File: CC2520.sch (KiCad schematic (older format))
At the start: 29 parts, among them P3 SMA_SMD, U6 CC2520, U7 CC2592, X1 32Mhz

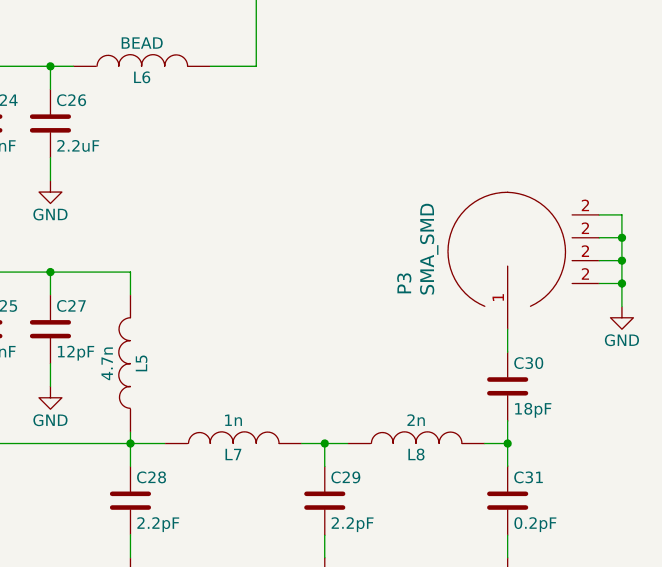
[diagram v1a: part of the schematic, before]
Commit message: tuned rf
added u.fl connectors to tune line 
moved some lines under rf components
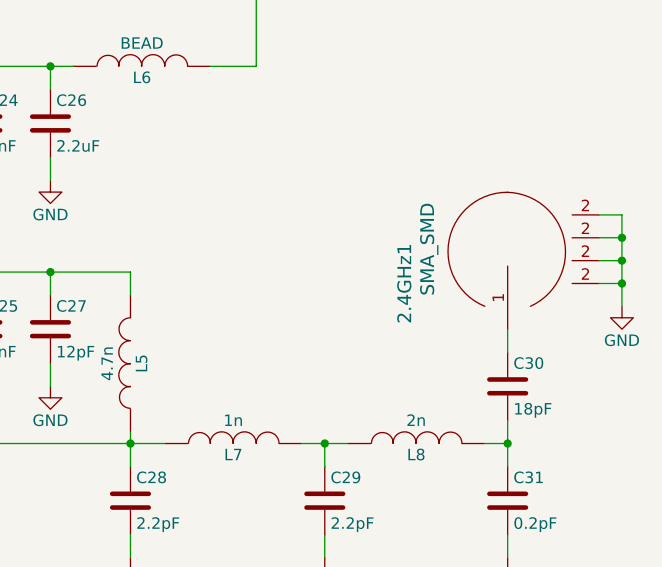
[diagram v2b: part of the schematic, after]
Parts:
- C20, C23, C26, C28, C29: footprint Capacitors_SMD:C_0402 -> Capacitor_SMD:C_0603_1608Metric
- C22, C27: footprint Capacitors_SMD:C_0402 -> Capacitor_SMD:C_1210_3225Metric
- renumbered P3 to 2.4GHz1
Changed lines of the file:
@@
 $EndComp
 $Comp
-L GND #PWR078
+L GND #PWR079
 U 1 1 5AF17357
 P 3350 1700
-F 0 "#PWR078" H 3350 1450 50  0001 C CNN
+F 0 "#PWR079" H 3350 1450 50  0001 C CNN
 F 1 "GND" H 3350 1550 50  0000 C CNN
 F 2 "" H 3350 1700 50  0001 C CNN
@@
 $EndComp
 $Comp
-L GND #PWR079
+L GND #PWR080
 U 1 1 5AF17476
 P 3700 1700
-F 0 "#PWR079" H 3700 1450 50  0001 C CNN
+F 0 "#PWR080" H 3700 1450 50  0001 C CNN
 F 1 "GND" H 3700 1550 50  0000 C CNN
 F 2 "" H 3700 1700 50  0001 C CNN
@@
 $EndComp
 $Comp
-L GND #PWR080
+L GND #PWR081
 U 1 1 5AF174E2
 P 4050 1700
-F 0 "#PWR080" H 4050 1450 50  0001 C CNN
+F 0 "#PWR081" H 4050 1450 50  0001 C CNN
 F 1 "GND" H 4050 1550 50  0000 C CNN
 F 2 "" H 4050 1700 50  0001 C CNN
@@
 F 0 "C20" H 4375 1600 50  0000 L CNN
 F 1 "2.2uF" H 4375 1400 50  0000 L CNN
-F 2 "Capacitors_SMD:C_0402" H 4388 1350 50  0001 C CNN
+F 2 "Capacitor_SMD:C_0603_1608Metric" H 4388 1350 50  0001 C CNN
 F 3 "" H 4350 1500 50  0001 C CNN
 	1    4350 1500
@@
 $EndComp
 $Comp
-L GND #PWR081
+L GND #PWR082
 U 1 1 5AF17781
 P 4350 1700
-F 0 "#PWR081" H 4350 1450 50  0001 C CNN
+F 0 "#PWR082" H 4350 1450 50  0001 C CNN
 F 1 "GND" H 4350 1550 50  0000 C CNN
 F 2 "" H 4350 1700 50  0001 C CNN
@@
 $EndComp
 $Comp
-L GND #PWR082
+L GND #PWR083
 U 1 1 5AF17924
 P 3200 4700
-F 0 "#PWR082" H 3200 4450 50  0001 C CNN
+F 0 "#PWR083" H 3200 4450 50  0001 C CNN
 F 1 "GND" H 3200 4550 50  0000 C CNN
 F 2 "" H 3200 4700 50  0001 C CNN
@@
 $EndComp
 $Comp
-L GND #PWR083
+L GND #PWR084
 U 1 1 5AF17A42
 P 3600 4850
-F 0 "#PWR083" H 3600 4600 50  0001 C CNN
+F 0 "#PWR084" H 3600 4600 50  0001 C CNN
 F 1 "GND" H 3600 4700 50  0000 C CNN
 F 2 "" H 3600 4850 50  0001 C CNN
@@
 $EndComp
 $Comp
-L GND #PWR084
+L GND #PWR085
 U 1 1 5AF17F39
 P 4200 4850
-F 0 "#PWR084" H 4200 4600 50  0001 C CNN
+F 0 "#PWR085" H 4200 4600 50  0001 C CNN
 F 1 "GND" H 4200 4700 50  0000 C CNN
 F 2 "" H 4200 4850 50  0001 C CNN
@@
 $EndComp
 $Comp
-L GND #PWR085
+L GND #PWR086
 U 1 1 5AF1813C
 P 3900 4650
-F 0 "#PWR085" H 3900 4400 50  0001 C CNN
+F 0 "#PWR086" H 3900 4400 50  0001 C CNN
 F 1 "GND" H 3900 4500 50  0000 C CNN
 F 2 "" H 3900 4650 50  0001 C CNN
@@
 LNA_EN
 $Comp
-L GND #PWR086
+L GND #PWR087
 U 1 1 5AF19B73
 P 4500 4250
-F 0 "#PWR086" H 4500 4000 50  0001 C CNN
+F 0 "#PWR087" H 4500 4000 50  0001 C CNN
 F 1 "GND" H 4500 4100 50  0000 C CNN
 F 2 "" H 4500 4250 50  0001 C CNN
@@
 NoConn ~ 3100 2950
 $Comp
-L GND #PWR087
+L GND #PWR088
 U 1 1 5AF1A852
 P 1700 4300
-F 0 "#PWR087" H 1700 4050 50  0001 C CNN
+F 0 "#PWR088" H 1700 4050 50  0001 C CNN
 F 1 "GND" H 1700 4150 50  0000 C CNN
 F 2 "" H 1700 4300 50  0001 C CNN
@@
 LNA_EN
 $Comp
-L GND #PWR088
+L GND #PWR089
 U 1 1 5AF1AD36
 P 5300 4400
-F 0 "#PWR088" H 5300 4150 50  0001 C CNN
+F 0 "#PWR089" H 5300 4150 50  0001 C CNN
 F 1 "GND" H 5300 4250 50  0000 C CNN
 F 2 "" H 5300 4400 50  0001 C CNN
@@
 $EndComp
 $Comp
-L GND #PWR089
+L GND #PWR090
 U 1 1 5AF1B0D0
 P 6650 4400
-F 0 "#PWR089" H 6650 4150 50  0001 C CNN
+F 0 "#PWR090" H 6650 4150 50  0001 C CNN
 F 1 "GND" H 6650 4250 50  0000 C CNN
 F 2 "" H 6650 4400 50  0001 C CNN
@@
 $EndComp
 $Comp
-L GND #PWR090
+L GND #PWR091
 U 1 1 5AF1B236
 P 5050 4450
-F 0 "#PWR090" H 5050 4200 50  0001 C CNN
+F 0 "#PWR091" H 5050 4200 50  0001 C CNN
 F 1 "GND" H 5050 4300 50  0000 C CNN
 F 2 "" H 5050 4450 50  0001 C CNN
@@
 $EndComp
 $Comp
-L SMA_SMD P3
+L SMA_SMD 2.4GHz1
 U 1 1 5AF1C19E
 P 9600 3000
-F 0 "P3" H 9550 3450 60  0000 C CNN
+F 0 "2.4GHz1" H 9550 3450 60  0000 C CNN
 F 1 "SMA_SMD" H 9700 3350 60  0000 C CNN
 F 2 "Connectors:SMA_THT_Jack_Straight" H 9700 3550 60  0001 C CNN
@@
 F 0 "C23" H 7025 3350 50  0000 L CNN
 F 1 "2.2uF" H 7025 3150 50  0000 L CNN
-F 2 "Capacitors_SMD:C_0402" H 7038 3100 50  0001 C CNN
+F 2 "Capacitor_SMD:C_0603_1608Metric" H 7038 3100 50  0001 C CNN
 F 3 "" H 7000 3250 50  0001 C CNN
 	1    7000 3250
@@
 F 0 "C27" H 7625 3350 50  0000 L CNN
 F 1 "12pF" H 7625 3150 50  0000 L CNN
-F 2 "Capacitors_SMD:C_0402" H 7638 3100 50  0001 C CNN
+F 2 "Capacitor_SMD:C_1210_3225Metric" H 7638 3100 50  0001 C CNN
 F 3 "" H 7600 3250 50  0001 C CNN
 	1    7600 3250
@@
 F 0 "C28" H 7975 4100 50  0000 L CNN
 F 1 "2.2pF" H 7975 3900 50  0000 L CNN
-F 2 "Capacitors_SMD:C_0402" H 7988 3850 50  0001 C CNN
+F 2 "Capacitor_SMD:C_0603_1608Metric" H 7988 3850 50  0001 C CNN
 F 3 "" H 7950 4000 50  0001 C CNN
 	1    7950 4000
@@
 F 0 "C29" H 8825 4100 50  0000 L CNN
 F 1 "2.2pF" H 8825 3900 50  0000 L CNN
-F 2 "Capacitors_SMD:C_0402" H 8838 3850 50  0001 C CNN
+F 2 "Capacitor_SMD:C_0603_1608Metric" H 8838 3850 50  0001 C CNN
 F 3 "" H 8800 4000 50  0001 C CNN
 	1    8800 4000
@@
 $EndComp
 $Comp
-L GND #PWR091
+L GND #PWR092
 U 1 1 5AF1D3FB
 P 7000 3500
-F 0 "#PWR091" H 7000 3250 50  0001 C CNN
+F 0 "#PWR092" H 7000 3250 50  0001 C CNN
 F 1 "GND" H 7000 3350 50  0000 C CNN
 F 2 "" H 7000 3500 50  0001 C CNN
@@
 $EndComp
 $Comp
-L GND #PWR092
+L GND #PWR093
 U 1 1 5AF1D441
 P 7300 3500
-F 0 "#PWR092" H 7300 3250 50  0001 C CNN
+F 0 "#PWR093" H 7300 3250 50  0001 C CNN
 F 1 "GND" H 7300 3350 50  0000 C CNN
 F 2 "" H 7300 3500 50  0001 C CNN
@@
 $EndComp
 $Comp
-L GND #PWR093
+L GND #PWR094
 U 1 1 5AF1D487
 P 7600 3500
-F 0 "#PWR093" H 7600 3250 50  0001 C CNN
+F 0 "#PWR094" H 7600 3250 50  0001 C CNN
 F 1 "GND" H 7600 3350 50  0000 C CNN
 F 2 "" H 7600 3500 50  0001 C CNN
@@
 $EndComp
 $Comp
-L GND #PWR094
+L GND #PWR095
 U 1 1 5AF1DC67
 P 7950 4250
-F 0 "#PWR094" H 7950 4000 50  0001 C CNN
+F 0 "#PWR095" H 7950 4000 50  0001 C CNN
 F 1 "GND" H 7950 4100 50  0000 C CNN
 F 2 "" H 7950 4250 50  0001 C CNN
@@
 $EndComp
 $Comp
-L GND #PWR095
+L GND #PWR096
 U 1 1 5AF1DCAD
 P 8800 4250
-F 0 "#PWR095" H 8800 4000 50  0001 C CNN
+F 0 "#PWR096" H 8800 4000 50  0001 C CNN
 F 1 "GND" H 8800 4100 50  0000 C CNN
 F 2 "" H 8800 4250 50  0001 C CNN
@@
 $EndComp
 $Comp
-L GND #PWR096
+L GND #PWR097
 U 1 1 5AF1DCF3
 P 9600 4250
-F 0 "#PWR096" H 9600 4000 50  0001 C CNN
+F 0 "#PWR097" H 9600 4000 50  0001 C CNN
 F 1 "GND" H 9600 4100 50  0000 C CNN
 F 2 "" H 9600 4250 50  0001 C CNN
@@
 $EndComp
 $Comp
-L GND #PWR097
+L GND #PWR098
 U 1 1 5AF1E105
 P 10100 3150
-F 0 "#PWR097" H 10100 2900 50  0001 C CNN
+F 0 "#PWR098" H 10100 2900 50  0001 C CNN
 F 1 "GND" H 10100 3000 50  0000 C CNN
 F 2 "" H 10100 3150 50  0001 C CNN
@@
 F 0 "C22" H 7025 2450 50  0000 L CNN
 F 1 "12uF" H 7025 2250 50  0000 L CNN
-F 2 "Capacitors_SMD:C_0402" H 7038 2200 50  0001 C CNN
+F 2 "Capacitor_SMD:C_1210_3225Metric" H 7038 2200 50  0001 C CNN
 F 3 "" H 7000 2350 50  0001 C CNN
 	1    7000 2350
@@
 F 0 "C26" H 7625 2450 50  0000 L CNN
 F 1 "2.2uF" H 7625 2250 50  0000 L CNN
-F 2 "Capacitors_SMD:C_0402" H 7638 2200 50  0001 C CNN
+F 2 "Capacitor_SMD:C_0603_1608Metric" H 7638 2200 50  0001 C CNN
 F 3 "" H 7600 2350 50  0001 C CNN
 	1    7600 2350
@@
 $EndComp
 $Comp
-L GND #PWR098
+L GND #PWR099
 U 1 1 5AF1EEB5
 P 7000 2600
-F 0 "#PWR098" H 7000 2350 50  0001 C CNN
+F 0 "#PWR099" H 7000 2350 50  0001 C CNN
 F 1 "GND" H 7000 2450 50  0000 C CNN
 F 2 "" H 7000 2600 50  0001 C CNN
@@
 $EndComp
 $Comp
-L GND #PWR099
+L GND #PWR0100
 U 1 1 5AF1EEBB
 P 7300 2600
-F 0 "#PWR099" H 7300 2350 50  0001 C CNN
+F 0 "#PWR0100" H 7300 2350 50  0001 C CNN
 F 1 "GND" H 7300 2450 50  0000 C CNN
 F 2 "" H 7300 2600 50  0001 C CNN
@@
 $EndComp
 $Comp
-L GND #PWR0100
+L GND #PWR0101
 U 1 1 5AF1EEC1
 P 7600 2600
-F 0 "#PWR0100" H 7600 2350 50  0001 C CNN
+F 0 "#PWR0101" H 7600 2350 50  0001 C CNN
 F 1 "GND" H 7600 2450 50  0000 C CNN
 F 2 "" H 7600 2600 50  0001 C CNN
@@
 	6650 2100 6650 3550
 $Comp
-L +3V3 #PWR0101
+L +3V3 #PWR0102
 U 1 1 5AF27FCB
 P 8500 1800
-F 0 "#PWR0101" H 8500 1650 50  0001 C CNN
+F 0 "#PWR0102" H 8500 1650 50  0001 C CNN
 F 1 "+3V3" H 8500 1940 50  0000 C CNN
 F 2 "" H 8500 1800 50  0001 C CNN
@@
 $EndComp
 $Comp
-L +3V3 #PWR0102
+L +3V3 #PWR0103
 U 1 1 5AF27F7D
 P 5900 900
-F 0 "#PWR0102" H 5900 750 50  0001 C CNN
+F 0 "#PWR0103" H 5900 750 50  0001 C CNN
 F 1 "+3V3" H 5900 1040 50  0000 C CNN
 F 2 "" H 5900 900 50  0001 C CNN
